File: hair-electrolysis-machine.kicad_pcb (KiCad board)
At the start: 2 copper layers, 53 x 53 mm, 83 parts, among them J1 Conn_01x04_Pin, J2 USB_C_Receptacle_USB2.0_16P, J3 AudioJack2_Ground_Switch, J4 Conn_01x04_Pin, J5 Conn_01x04_Pin, J6 AudioJack2_Ground_Switch, J7 AudioJack2_Ground_Switch, Q1 BSS138, SW1 SW_SPDT, SW2 BTN, SW3 BTN, SW4 RotaryEncoder_Switch, SW5 BTN, U1 TP4054, U2 XC6206PxxxMR, U3 LM358B, U4 STM32G0B1RBTx

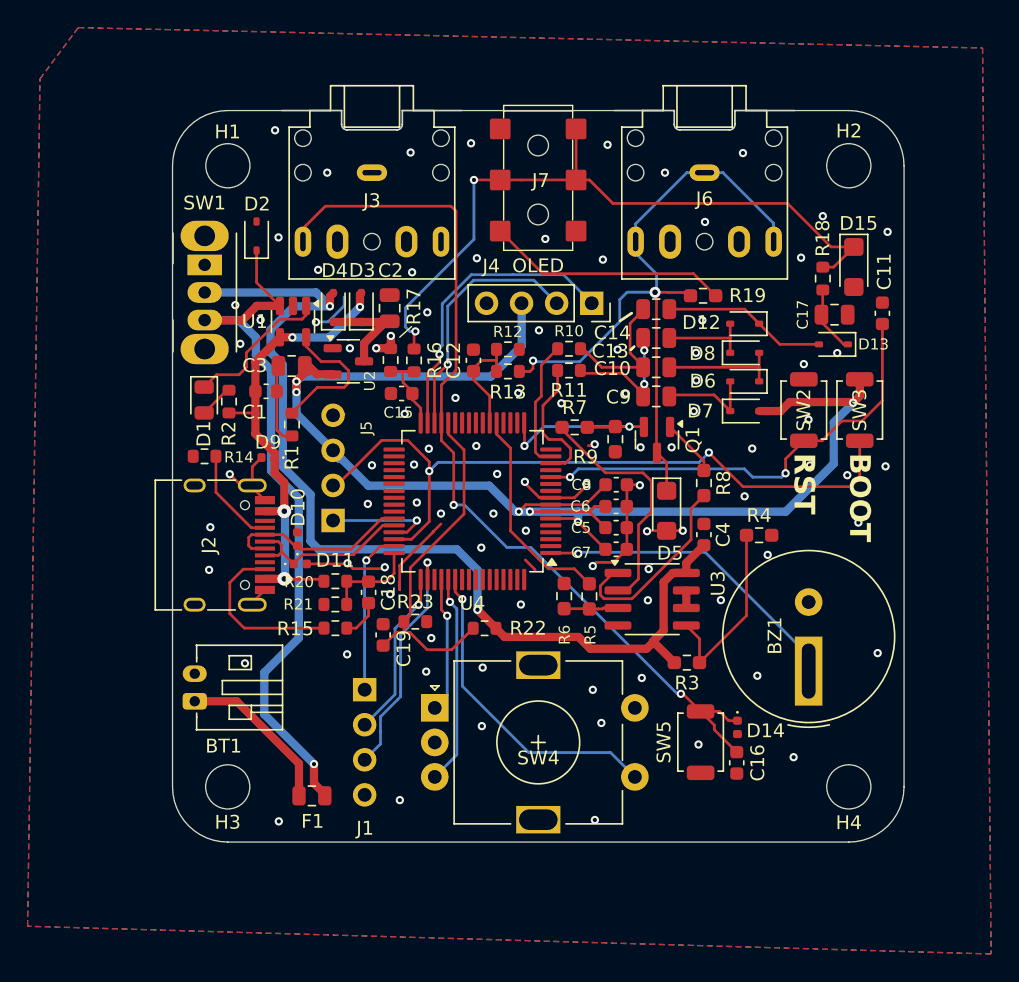
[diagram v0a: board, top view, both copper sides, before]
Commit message: Updated buzzer and jack detection
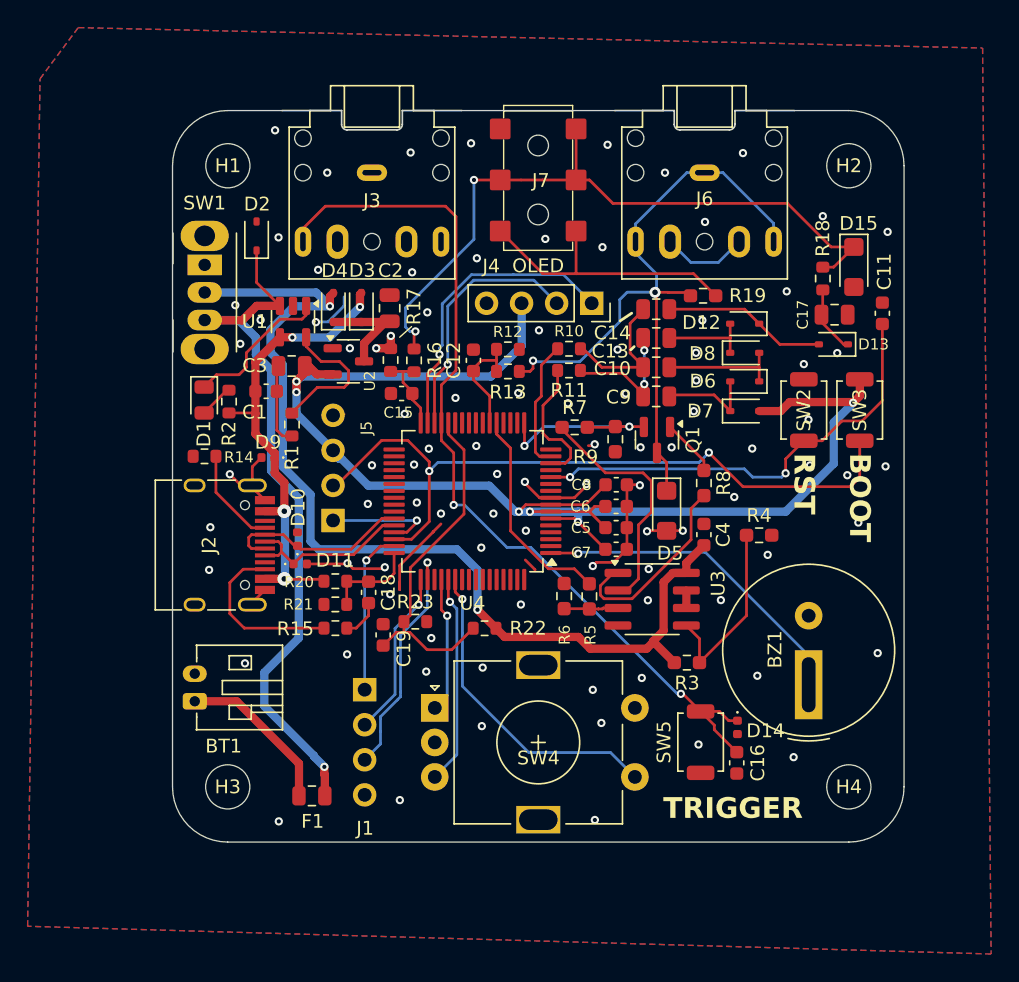
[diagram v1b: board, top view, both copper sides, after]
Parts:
- moved BZ1 0.99 mm to (169.1, 112.6)
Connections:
- J6 pad RN: unconnected-(J6-PadRN) -> Net-(J6-PadRN)
- J6 pad TN: unconnected-(J6-PadTN) -> Net-(J6-PadRN)
- J7 pad RN: unconnected-(J7-PadRN) -> Net-(J7-PadRN)
- J7 pad TN: Net-(J7-PadTN) -> Net-(J7-PadRN)
- R19 pad 1: Net-(J7-PadTN) -> Net-(J7-PadRN)
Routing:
- net Net-(J7-PadRN): track 0.00 -> 20.6 mm
- net Net-(J7-PadTN): track 17.6 -> 0.00 mm
- net Net-(J6-PadRN): track 0.00 -> 6.24 mm
- net /Mcu/BUZZER1: track 26.8 -> 27.8 mm
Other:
- board text added: "TRIGGER"
- board text removed: "Mod me here!"
